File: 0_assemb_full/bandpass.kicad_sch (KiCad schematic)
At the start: 26 parts, among them U1 LM2902, U3 LM2902

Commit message: A lot of work done on the STM32 PCB layout.
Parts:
- added TP8: BP_LP, TestPoint:TestPoint_THTPad_1.5x1.5mm_Drill0.7mm, symbol Connector:TestPoint
- added TP9: BP_HP, TestPoint:TestPoint_THTPad_1.5x1.5mm_Drill0.7mm, symbol Connector:TestPoint
- C3, C4, C5, C7: footprint (none) -> Capacitor_THT:C_Rect_L7.0mm_W4.5mm_P5.00mm
- C6: footprint (none) -> Capacitor_SMD:CP_Elec_5x5.4
- R1, R10, R12, R13, R14, R15, R16, R17, R18, R19, R2, R3, R4, R5, R6, R7, R8, R9: footprint (none) -> Resistor_SMD:R_0805_2012Metric_Pad1.20x1.40mm_HandSolder
- R11: value 124 -> 120; footprint (none) -> Resistor_SMD:R_0805_2012Metric_Pad1.20x1.40mm_HandSolder
- U1, U3: footprint (none) -> Package_DIP:DIP-14_W7.62mm
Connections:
- net LP Pre-LP: now also TP8.1
- net at C3.1, R6.2, U1.10 (+)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: now also TP9.1

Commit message: Some filter adjustments
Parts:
- added C52: 100n, Capacitor_SMD:C_0805_2012Metric_Pad1.18x1.45mm_HandSolder, symbol Device:C_Small
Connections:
- net 5V: now also C52.1
- net GND: now also C52.2
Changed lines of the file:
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@@
   (junction (at 72.39 86.36) (diameter 0) (color 0 0 0 0)
   )
+  (junction (at 72.39 39.37) (diameter 0) (color 0 0 0 0)
+  )
   (junction (at 247.65 143.51) (diameter 0) (color 0 0 0 0)
   )
@@
     (stroke (width 0) (type default) (color 0 0 0 0))
   )
+  (wire (pts (xy 82.55 39.37) (xy 78.74 39.37))
+    (stroke (width 0) (type default) (color 0 0 0 0))
+  )
+  (wire (pts (xy 72.39 39.37) (xy 73.66 39.37))
+    (stroke (width 0) (type default) (color 0 0 0 0))
+  )
   (wire (pts (xy 184.15 53.34) (xy 184.15 58.42))
     (stroke (width 0) (type default) (color 0 0 0 0))
@@
     (stroke (width 0) (type default) (color 0 0 0 0))
   )
+  (wire (pts (xy 72.39 39.37) (xy 72.39 43.18))
+    (stroke (width 0) (type default) (color 0 0 0 0))
+  )
   (wire (pts (xy 160.02 69.85) (xy 184.15 69.85))
     (stroke (width 0) (type default) (color 0 0 0 0))
@@
     (stroke (width 0) (type default) (color 0 0 0 0))
   )
+  (wire (pts (xy 82.55 40.64) (xy 82.55 39.37))
+    (stroke (width 0) (type default) (color 0 0 0 0))
+  )
   (wire (pts (xy 142.24 50.8) (xy 143.51 50.8))
     (stroke (width 0) (type default) (color 0 0 0 0))
@@
   )
   (wire (pts (xy 148.59 86.36) (xy 184.15 86.36))
+    (stroke (width 0) (type default) (color 0 0 0 0))
+  )
+  (wire (pts (xy 72.39 36.83) (xy 72.39 39.37))
     (stroke (width 0) (type default) (color 0 0 0 0))
   )
@@
     )
   )
-  (global_label "5V" (shape input) (at 72.39 43.18 90) (fields_autoplaced)
-    (effects (font (size 1.27 1.27)) (justify left))
-    (property "Intersheet References" "${INTERSHEET_REFS}" (id 0) (at 72.3106 38.4688 90)
-      (effects (font (size 1.27 1.27)) (justify left) hide)
+  (global_label "5V" (shape input) (at 72.39 36.83 180) (fields_autoplaced)
+    (effects (font (size 1.27 1.27)) (justify right))
+    (property "Intersheet References" "${INTERSHEET_REFS}" (id 0) (at 67.6788 36.9094 0)
+      (effects (font (size 1.27 1.27)) (justify right) hide)
     )
   )
@@
     (pin "2")
   )
+  (symbol (lib_id "power:GND") (at 82.55 40.64 0) (unit 1)
+    (in_bom yes) (on_board yes) (fields_autoplaced)
+    (property "Reference" "#PWR047" (id 0) (at 82.55 46.99 0)
+      (effects (font (size 1.27 1.27)) hide)
+    )
+    (property "Value" "GND" (id 1) (at 82.55 45.72 0)
+      (effects (font (size 1.27 1.27)) hide)
+    )
+    (property "Footprint" "" (id 2) (at 82.55 40.64 0)
+      (effects (font (size 1.27 1.27)) hide)
+    )
+    (property "Datasheet" "" (id 3) (at 82.55 40.64 0)
+      (effects (font (size 1.27 1.27)) hide)
+    )
+    (pin "1")
+  )
   (symbol (lib_id "Device:R_US") (at 143.51 58.42 180) (unit 1)
     (in_bom yes) (on_board yes) (fields_autoplaced)
@@
       (effects (font (size 1.27 1.27)) hide)
     )
+    (pin "1")
+    (pin "2")
+  )
+  (symbol (lib_id "Device:C_Small") (at 76.2 39.37 90) (unit 1)
+    (in_bom yes) (on_board yes) (fields_autoplaced)
+    (property "Reference" "C52" (id 0) (at 76.2063 33.02 90))
+    (property "Value" "100n" (id 1) (at 76.2063 35.56 90))
+    (property "Footprint" "Capacitor_SMD:C_0805_2012Metric_Pad1.18x1.45mm_HandSolder" (id 2) (at 76.2 39.37 0)
+      (effects (font (size 1.27 1.27)) hide)
+    )
+    (property "Datasheet" "~" (id 3) (at 76.2 39.37 0)
+      (effects (font (size 1.27 1.27)) hide)
+    )

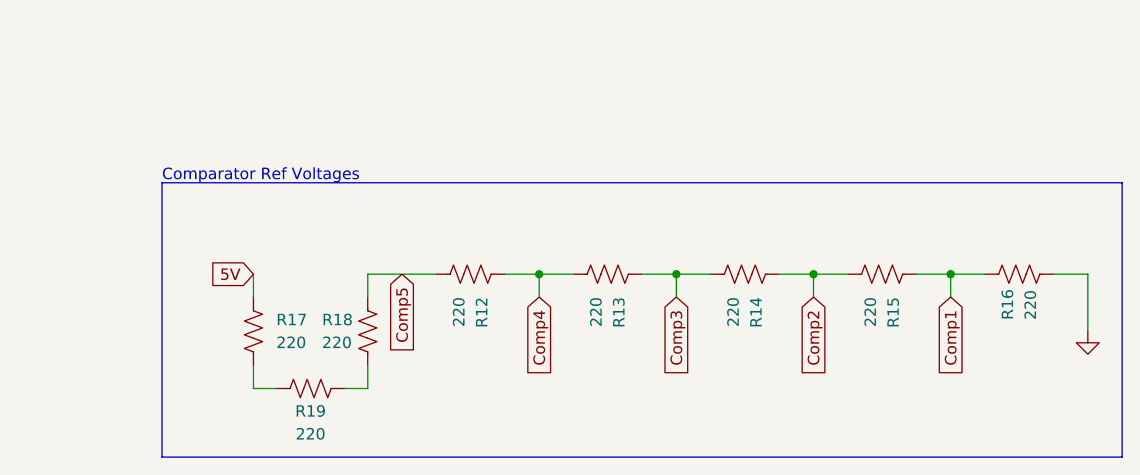
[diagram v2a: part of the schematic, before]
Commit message: Active Filters layout added
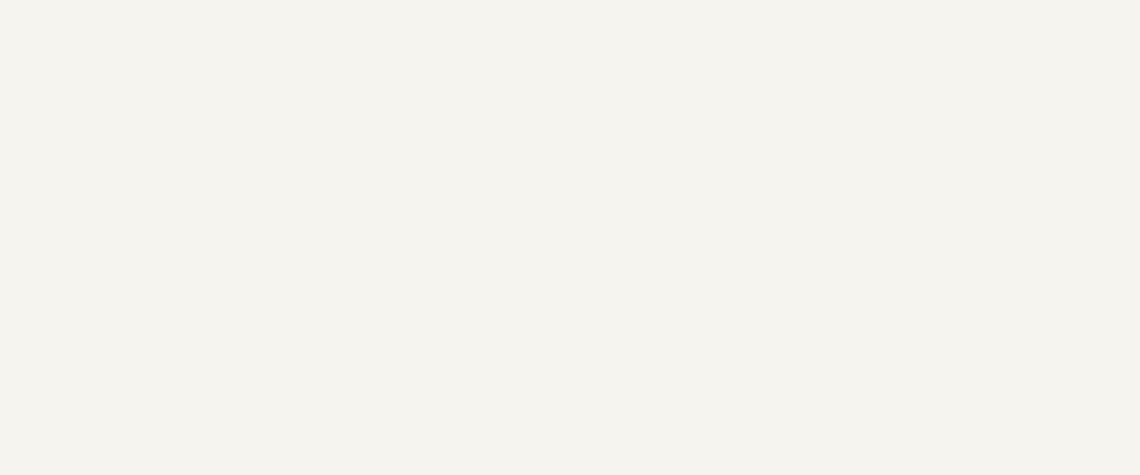
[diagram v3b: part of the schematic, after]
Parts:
- removed R12, R13, R14, R15, R16, R17, R18, R19: 220, Resistor_SMD:R_0805_2012Metric_Pad1.20x1.40mm_HandSolder, symbol Device:R_US
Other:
- note removed: "Comparator Ref Voltages"
- title: Band Pass Filter with Bar Graph LEDs -> Band Pass Filter

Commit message: Made adjustments according to presentation feedback. Almost ready for teaching team to look over.
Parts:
- TP8, TP9: footprint TestPoint:TestPoint_THTPad_1.5x1.5mm_Drill0.7mm -> TestPoint:TestPoint_THTPad_2.0x2.0mm_Drill1.0mm
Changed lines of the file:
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@@
       (effects (font (size 1.27 1.27)) (justify left))
     )
-    (property "Footprint" "TestPoint:TestPoint_THTPad_1.5x1.5mm_Drill0.7mm" (id 2) (at 96.52 50.8 0)
+    (property "Footprint" "TestPoint:TestPoint_THTPad_2.0x2.0mm_Drill1.0mm" (id 2) (at 96.52 50.8 0)
       (effects (font (size 1.27 1.27)) hide)
     )
@@
       (effects (font (size 1.27 1.27)) (justify left))
     )
-    (property "Footprint" "TestPoint:TestPoint_THTPad_1.5x1.5mm_Drill0.7mm" (id 2) (at 151.13 50.8 0)
+    (property "Footprint" "TestPoint:TestPoint_THTPad_2.0x2.0mm_Drill1.0mm" (id 2) (at 151.13 50.8 0)
       (effects (font (size 1.27 1.27)) hide)
     )
